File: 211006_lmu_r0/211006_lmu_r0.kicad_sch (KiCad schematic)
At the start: 6 parts, among them J1 Conn_02x03_Odd_Even, J10 LOWER_BANK, J2 Conn_02x03_Odd_Even, J3 Conn_02x08_Odd_Even, J4 UPPER_BANK, J8 Conn_01x02

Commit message: routed ltc3811 accessories
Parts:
- J8: footprint Connector_PinHeader_2.54mm:PinHeader_1x02_P2.54mm_Vertical -> Connector_Molex:Molex_Mini-Fit_Jr_5566-02A_2x01_P4.20mm_Vertical
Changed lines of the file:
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@@
     (property "Reference" "J8" (id 0) (at 46.5328 118.745 0))
     (property "Value" "Conn_01x02" (id 1) (at 46.5328 121.0564 0))
-    (property "Footprint" "Connector_PinHeader_2.54mm:PinHeader_1x02_P2.54mm_Vertical" (id 2) (at 44.45 127 0)
+    (property "Footprint" "Connector_Molex:Molex_Mini-Fit_Jr_5566-02A_2x01_P4.20mm_Vertical" (id 2) (at 44.45 127 0)
       (effects (font (size 1.27 1.27)) hide)
     )
@@
       (reference "#PWR079") (unit 1) (value "GND_ISO") (footprint "")
     )
-    (path "/00000000-0000-0000-0000-0000615d6dd3/00000000-0000-0000-0000-000061f5a303"
-      (reference "#PWR080") (unit 1) (value "GND_ISO") (footprint "")
-    )
     (path "/00000000-0000-0000-0000-0000615d6dd3/00000000-0000-0000-0000-000061686b7b"
       (reference "#PWR081") (unit 1) (value "GND_ISO") (footprint "")
@@
       (reference "#PWR0106") (unit 1) (value "+3V3_ISO") (footprint "")
     )
+    (path "/00000000-0000-0000-0000-0000615d6dd3/96582176-678b-48a1-974e-e2f11358f1e9"
+      (reference "#PWR0107") (unit 1) (value "+3V3_ISO") (footprint "")
+    )
     (path "/00000000-0000-0000-0000-00006171146a/00000000-0000-0000-0000-0000616c8099/f39239ac-c5ca-45ed-acd9-be3ff97551b4"
       (reference "#PWR0119") (unit 1) (value "+5V_HV") (footprint "")
@@
     )
     (path "/98658dae-a964-4b9c-a7f3-2277d461bf25"
-      (reference "J8") (unit 1) (value "Conn_01x02") (footprint "Connector_PinHeader_2.54mm:PinHeader_1x02_P2.54mm_Vertical")
+      (reference "J8") (unit 1) (value "Conn_01x02") (footprint "Connector_Molex:Molex_Mini-Fit_Jr_5566-02A_2x01_P4.20mm_Vertical")
     )
     (path "/00000000-0000-0000-0000-000061643001/00000000-0000-0000-0000-000061f4ce6c"

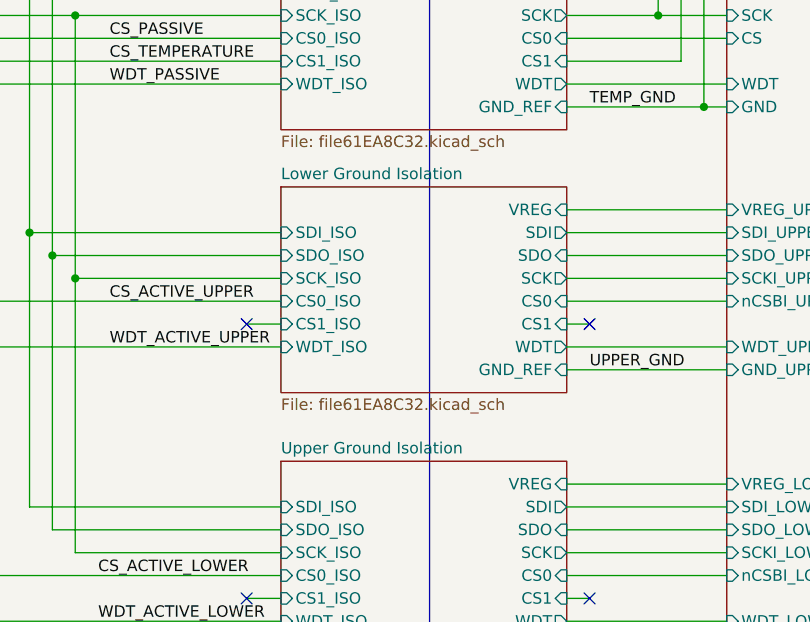
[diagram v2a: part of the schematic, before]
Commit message: Routed vehicle section
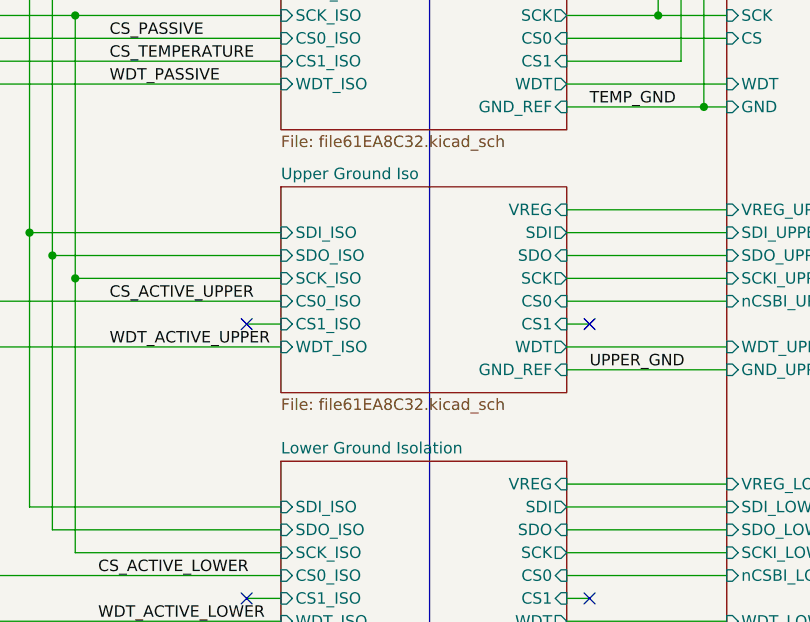
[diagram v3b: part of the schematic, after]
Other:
- removed sheet Upper Ground Isolation
- added sheet Upper Ground Iso (file61EA8C32.kicad_sch)
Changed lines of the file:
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@@
     (stroke (width 0) (type solid) (color 0 0 0 0))
     (fill (color 0 0 0 0.0000))
-    (property "Sheet name" "Upper Ground Isolation" (id 0) (at 179.07 128.8284 0)
+    (property "Sheet name" "Lower Ground Isolation" (id 0) (at 179.07 128.8284 0)
       (effects (font (size 1.27 1.27)) (justify left bottom))
     )
@@
     (stroke (width 0) (type solid) (color 0 0 0 0))
     (fill (color 0 0 0 0.0000))
-    (property "Sheet name" "Lower Ground Isolation" (id 0) (at 179.07 98.3484 0)
+    (property "Sheet name" "Upper Ground Iso" (id 0) (at 179.07 98.3484 0)
       (effects (font (size 1.27 1.27)) (justify left bottom))
     )
@@
       (reference "#PWR012") (unit 1) (value "+5V") (footprint "")
     )
-    (path "/00000000-0000-0000-0000-0000616ba638/00000000-0000-0000-0000-00006164f300"
-      (reference "#PWR013") (unit 1) (value "GND") (footprint "")
-    )
     (path "/00000000-0000-0000-0000-0000616ba638/00000000-0000-0000-0000-00006164cf50"
       (reference "#PWR014") (unit 1) (value "+3V3_ISO") (footprint "")
@@
       (reference "R4") (unit 1) (value "60R") (footprint "Resistor_SMD:R_0805_2012Metric_Pad1.20x1.40mm_HandSolder")
     )
-    (path "/00000000-0000-0000-0000-0000616ba638/00000000-0000-0000-0000-0000616603f3"
-      (reference "R5") (unit 1) (value "0R") (footprint "Resistor_SMD:R_0805_2012Metric_Pad1.20x1.40mm_HandSolder")
-    )
     (path "/00000000-0000-0000-0000-00006171146a/00000000-0000-0000-0000-0000616c8099/00000000-0000-0000-0000-000061f70d2c"

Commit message: started filling polygons
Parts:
- added R5: 0R, Resistor_SMD:R_0603_1608Metric_Pad0.98x0.95mm_HandSolder, symbol Device:R
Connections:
- net CAN_S: now also R5.2
- net VGND: now also R5.1
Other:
- note added: "ground to shield link"
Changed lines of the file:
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@@
+    (stroke (width 0) (type default) (color 0 0 0 0))
+  )
+  (wire (pts (xy 48.26 66.04) (xy 48.26 64.77))
     (stroke (width 0) (type default) (color 0 0 0 0))
   )
@@
     (stroke (width 0) (type default) (color 0 0 0 0))
   )
+  (wire (pts (xy 48.26 64.77) (xy 57.15 64.77))
+    (stroke (width 0) (type default) (color 0 0 0 0))
+  )
   (wire (pts (xy 151.13 74.93) (xy 147.32 74.93))
     (stroke (width 0) (type default) (color 0 0 0 0))
@@
     (stroke (width 0) (type default) (color 0 0 0 0))
   )
+  (wire (pts (xy 48.26 72.39) (xy 57.15 72.39))
+    (stroke (width 0) (type default) (color 0 0 0 0))
+  )
   (wire (pts (xy 228.6 101.6) (xy 210.82 101.6))
     (stroke (width 0) (type default) (color 0 0 0 0))
@@
     (stroke (width 0) (type default) (color 0 0 0 0))
   )
+  (wire (pts (xy 48.26 71.12) (xy 48.26 72.39))
+    (stroke (width 0) (type default) (color 0 0 0 0))
+  )
   (wire (pts (xy 41.91 71.12) (xy 48.26 71.12))
     (stroke (width 0) (type default) (color 0 0 0 0))
@@
   (wire (pts (xy 228.6 44.45) (xy 218.44 44.45))
     (stroke (width 0) (type default) (color 0 0 0 0))
+  )
+  (text "ground to shield link\n" (at 52.07 63.5 0)
+    (effects (font (size 1.27 1.27)) (justify left bottom))
   )
   (text "BYPASS" (at 31.75 90.17 0)
@@
     )
     (property "Manufacturer" "-" (id 5) (at 44.45 127 0)
+      (effects (font (size 1.27 1.27)) hide)
+    )
+    (pin "1")
+    (pin "2")
+  )
+  (symbol (lib_id "Device:R") (at 57.15 68.58 0) (unit 1)
+    (in_bom yes) (on_board yes)
+    (property "Reference" "R5" (id 0) (at 58.928 67.4116 0)
+      (effects (font (size 1.27 1.27)) (justify left))
+    )
+    (property "Value" "0R" (id 1) (at 58.928 69.723 0)
+      (effects (font (size 1.27 1.27)) (justify left))
+    )
+    (property "Footprint" "Resistor_SMD:R_0603_1608Metric_Pad0.98x0.95mm_HandSolder" (id 2) (at 55.372 68.58 90)
+      (effects (font (size 1.27 1.27)) hide)
+    )
+    (property "Datasheet" "~" (id 3) (at 57.15 68.58 0)
+      (effects (font (size 1.27 1.27)) hide)
+    )
+    (property "Part Number" "-" (id 4) (at 57.15 68.58 0)
+      (effects (font (size 1.27 1.27)) hide)
+    )
+    (property "Manufacturer" "-" (id 5) (at 57.15 68.58 0)
       (effects (font (size 1.27 1.27)) hide)
     )
@@
       (reference "R4") (unit 1) (value "60R") (footprint "Resistor_SMD:R_0805_2012Metric_Pad1.20x1.40mm_HandSolder")
     )
+    (path "/a228dd02-8caa-443f-9918-bbf6eb62d140"
+      (reference "R5") (unit 1) (value "0R") (footprint "Resistor_SMD:R_0603_1608Metric_Pad0.98x0.95mm_HandSolder")
+    )
     (path "/00000000-0000-0000-0000-00006171146a/00000000-0000-0000-0000-0000616c8099/00000000-0000-0000-0000-000061f70d2c"

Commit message: finished routing - beginning cleanup and review phase
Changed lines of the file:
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@@
   (no_connect (at 175.26 114.3))
   (no_connect (at 41.91 68.58))
-  (no_connect (at 213.36 114.3))
+  (no_connect (at 215.9 114.3))
   (no_connect (at 41.91 82.55))
   (wire (pts (xy 156.21 109.22) (xy 179.07 109.22))
@@
     (stroke (width 0) (type default) (color 0 0 0 0))
   )
-  (wire (pts (xy 228.6 132.08) (xy 210.82 132.08))
-    (stroke (width 0) (type default) (color 0 0 0 0))
-  )
   (wire (pts (xy 147.32 142.24) (xy 179.07 142.24))
     (stroke (width 0) (type default) (color 0 0 0 0))
@@
     (stroke (width 0) (type default) (color 0 0 0 0))
   )
+  (wire (pts (xy 226.06 132.08) (xy 228.6 132.08))
+    (stroke (width 0) (type default) (color 0 0 0 0))
+  )
   (wire (pts (xy 228.6 52.07) (xy 226.06 52.07))
     (stroke (width 0) (type default) (color 0 0 0 0))
@@
     (stroke (width 0) (type default) (color 0 0 0 0))
   )
+  (wire (pts (xy 213.36 72.39) (xy 213.36 132.08))
+    (stroke (width 0) (type default) (color 0 0 0 0))
+  )
   (wire (pts (xy 218.44 77.47) (xy 210.82 77.47))
     (stroke (width 0) (type default) (color 0 0 0 0))
   )
-  (wire (pts (xy 213.36 114.3) (xy 210.82 114.3))
+  (wire (pts (xy 215.9 114.3) (xy 210.82 114.3))
     (stroke (width 0) (type default) (color 0 0 0 0))
   )
@@
     (stroke (width 0) (type default) (color 0 0 0 0))
   )
+  (wire (pts (xy 210.82 132.08) (xy 213.36 132.08))
+    (stroke (width 0) (type default) (color 0 0 0 0))
+  )

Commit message: silkscreen changes, shifting bun leds
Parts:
- added H1, H2, H3: MountingHole, MountingHole:MountingHole_3.2mm_M3, symbol Mechanical:MountingHole

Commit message: started to export and fix things
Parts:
- H1, H2, H3, J4: Manufacturer (none) -> -; Part Number (none) -> -
- J10: Manufacturer (none) -> -
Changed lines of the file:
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@@
+      (effects (font (size 1.27 1.27)) hide)
+    )
+    (property "Manufacturer" "-" (id 4) (at 278.13 129.54 0)
       (effects (font (size 1.27 1.27)) hide)
     )
@@
       (effects (font (size 1.27 1.27)) hide)
     )
+    (property "Manufacturer" "-" (id 4) (at 19.05 27.94 0)
+      (effects (font (size 1.27 1.27)) hide)
+    )
+    (property "Part Number" "-" (id 5) (at 19.05 27.94 0)
+      (effects (font (size 1.27 1.27)) hide)
+    )
   )
   (symbol (lib_id "Connector_Generic:Conn_01x06") (at 278.13 88.9 0) (unit 1)
@@
     )
     (property "Datasheet" "~" (id 3) (at 278.13 88.9 0)
+      (effects (font (size 1.27 1.27)) hide)
+    )
+    (property "Manufacturer" "-" (id 4) (at 278.13 88.9 0)
+      (effects (font (size 1.27 1.27)) hide)
+    )
+    (property "Part Number" "-" (id 5) (at 278.13 88.9 0)
       (effects (font (size 1.27 1.27)) hide)
     )
@@
     )
     (property "Datasheet" "~" (id 3) (at 19.05 22.86 0)
+      (effects (font (size 1.27 1.27)) hide)
+    )
+    (property "Manufacturer" "-" (id 4) (at 19.05 22.86 0)
+      (effects (font (size 1.27 1.27)) hide)
+    )
+    (property "Part Number" "-" (id 5) (at 19.05 22.86 0)
       (effects (font (size 1.27 1.27)) hide)
     )
@@
       (effects (font (size 1.27 1.27)) hide)
     )
+    (property "Manufacturer" "-" (id 4) (at 19.05 17.78 0)
+      (effects (font (size 1.27 1.27)) hide)
+    )
+    (property "Part Number" "-" (id 5) (at 19.05 17.78 0)
+      (effects (font (size 1.27 1.27)) hide)
+    )
